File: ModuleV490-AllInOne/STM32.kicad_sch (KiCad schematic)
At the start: 46 parts, among them J1 SPI_DEBUG, J10 TEMP2, J11 TEMP1, J12 TEMP2, J13 TEMP3, J2 BOOT_MODE, J3 UART_PROG, J4 ST_LINK, J8 TXRX, Q1 AO3401A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

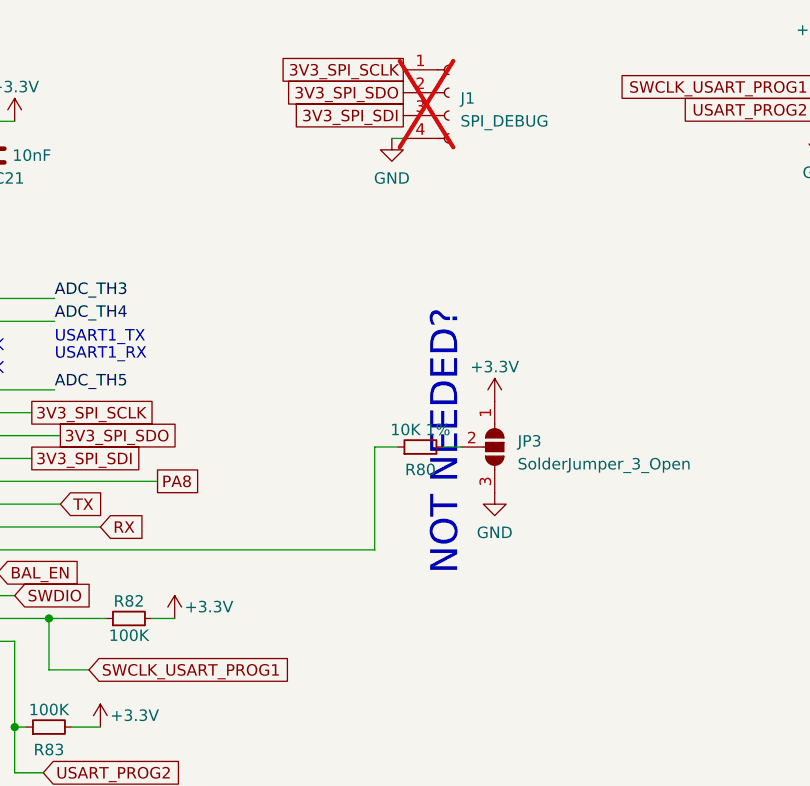
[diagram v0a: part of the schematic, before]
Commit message: Change JP1 jumper to single pin (remove part) and SPI debug pins
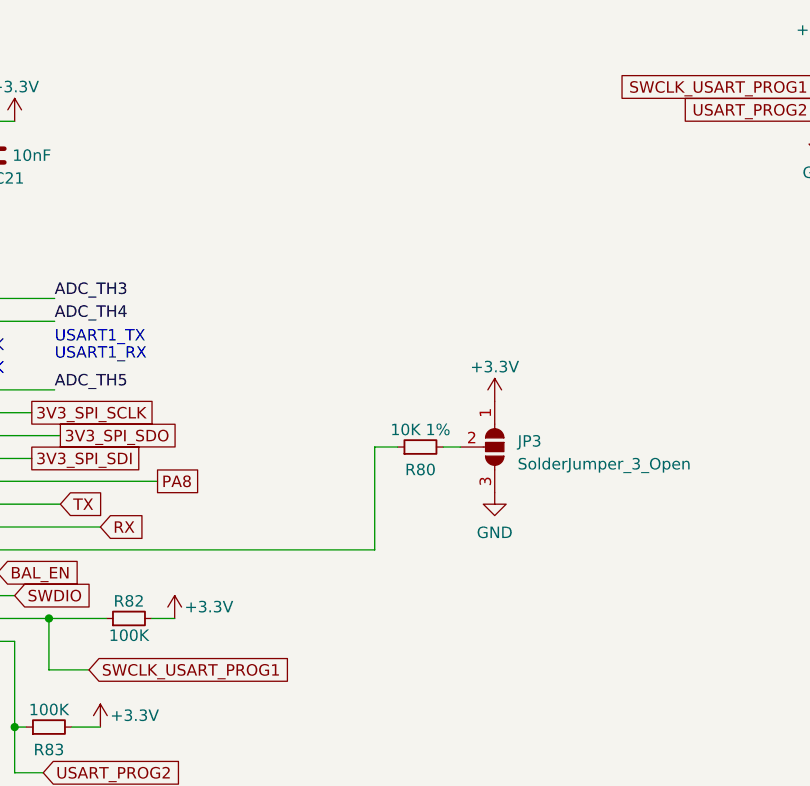
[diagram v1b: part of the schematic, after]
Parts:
- removed J1: SPI_DEBUG, Connector_PinSocket_2.00mm:PinSocket_1x04_P2.00mm_Vertical, symbol Connector:Conn_01x04_Socket
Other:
- note removed: "NOT NEEDED?"
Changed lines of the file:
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@@
-    (stroke (width 0) (type default))
-  )
-  (wire (pts (xy 140.97 46.99) (xy 142.24 46.99))
     (stroke (width 0) (type default))
   )
@@
     (effects (font (size 1.27 1.27)) (justify left bottom))
   )
-  (text "NOT NEEDED?" (at 148.59 66.04 90)
-    (effects (font (size 3 3)) (justify right bottom))
-  )
   (text "DRAIN" (at 126.365 144.78 0)
     (effects (font (size 1.27 1.27)) (justify left bottom))
@@
     )
   )
-  (global_label "3V3_SPI_SCLK" (shape passive) (at 142.24 39.37 180) (fields_autoplaced)
-    (effects (font (size 1.27 1.27)) (justify right))
-    (property "Intersheetrefs" "${INTERSHEET_REFS}" (at 127.1408 39.37 0)
-      (effects (font (size 1.27 1.27)) (justify right) hide)
-    )
-  )
   (global_label "USART_PROG2" (shape input) (at 102.235 117.475 0) (fields_autoplaced)
     (effects (font (size 1.27 1.27)) (justify left))
@@
     (property "Intersheetrefs" "${INTERSHEET_REFS}" (at 123.825 126.9896 90)
       (effects (font (size 1.27 1.27)) (justify left) hide)
-    )
-  )
-  (global_label "3V3_SPI_SDO" (shape passive) (at 142.24 41.91 180) (fields_autoplaced)
-    (effects (font (size 1.27 1.27)) (justify right))
-    (property "Intersheetrefs" "${INTERSHEET_REFS}" (at 128.1084 41.91 0)
-      (effects (font (size 1.27 1.27)) (justify right) hide)
-    )
-  )
-  (global_label "3V3_SPI_SDI" (shape passive) (at 142.24 44.45 180) (fields_autoplaced)
-    (effects (font (size 1.27 1.27)) (justify right))
-    (property "Intersheetrefs" "${INTERSHEET_REFS}" (at 128.8341 44.45 0)
-      (effects (font (size 1.27 1.27)) (justify right) hide)
     )
   )
@@
     )
   )
-  (symbol (lib_id "power:GND") (at 140.97 46.99 0) (unit 1)
-    (in_bom yes) (on_board yes) (dnp no) (fields_autoplaced)
-    (property "Reference" "#PWR035" (at 140.97 53.34 0)
-      (effects (font (size 1.27 1.27)) hide)
-    )
-    (property "Value" "GND" (at 140.97 51.435 0)
-      (effects (font (size 1.27 1.27)))
-    )
-    (property "Footprint" "" (at 140.97 46.99 0)
-      (effects (font (size 1.27 1.27)) hide)
-    )
-    (property "Datasheet" "" (at 140.97 46.99 0)
-      (effects (font (size 1.27 1.27)) hide)
-    )
-    (pin "1")
-    (instances
-      (project "Module_16S"
-        (path "/e63e39d7-6ac0-4ffd-8aa3-1841a4541b55/f65e9c34-bb90-4d0c-b988-67c6b9ba4d90"
-          (reference "#PWR035") (unit 1)
-        )
-      )
-    )
-  )
   (symbol (lib_id "power:+3.3V") (at 99.06 45.085 0) (unit 1)
     (in_bom yes) (on_board yes) (dnp no) (fields_autoplaced)
@@
         )
       )
-    )
-  )
-  (symbol (lib_id "Connector:Conn_01x04_Socket") (at 147.32 41.91 0) (unit 1)
-    (in_bom no) (on_board yes) (dnp yes) (fields_autoplaced)
-    (property "Reference" "J1" (at 148.59 42.545 0)
-      (effects (font (size 1.27 1.27)) (justify left))
-    )
-    (property "Value" "SPI_DEBUG" (at 148.59 45.085 0)
-      (effects (font (size 1.27 1.27)) (justify left))
-    )
-    (property "Footprint" "Connector_PinSocket_2.00mm:PinSocket_1x04_P2.00mm_Vertical" (at 147.32 41.91 0)
-      (effects (font (size 1.27 1.27)) hide)
-    )
-    (property "Datasheet" "~" (at 147.32 41.91 0)
-      (effects (font (size 1.27 1.27)) hide)
-    )
-    (property "PartNumber" "C2718488" (at 147.32 41.91 0)
-      (effects (font (size 1.27 1.27)) hide)
-    )
-    (property "LCSCStockCode" "C2718488" (at 147.32 41.91 0)
-      (effects (font (size 1.27 1.27)) hide)
-    )
-    (pin "1")
-    (pin "2")
-    (pin "3")
-    (pin "4")
-    (instances
-      (project "Module_16S"
-        (path "/e63e39d7-6ac0-4ffd-8aa3-1841a4541b55/f65e9c34-bb90-4d0c-b988-67c6b9ba4d90"
-          (reference "J1") (unit 1)
-        )
-      )
